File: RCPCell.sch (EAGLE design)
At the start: 28 parts, among them IC1 SIM900, U1 PESDXS4UD, U7 FAN8303

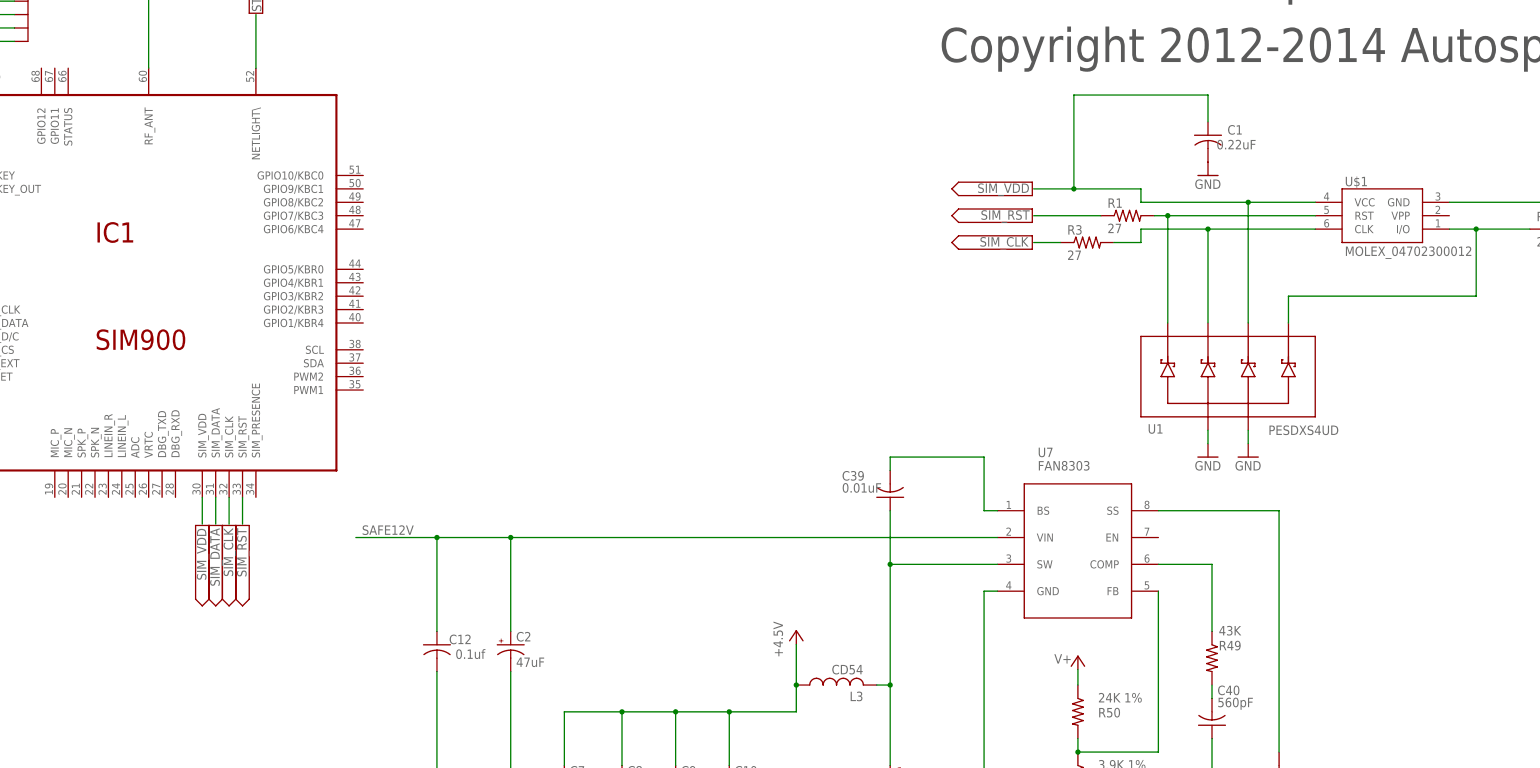
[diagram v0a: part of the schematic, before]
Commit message: flipped components on cell module to top side
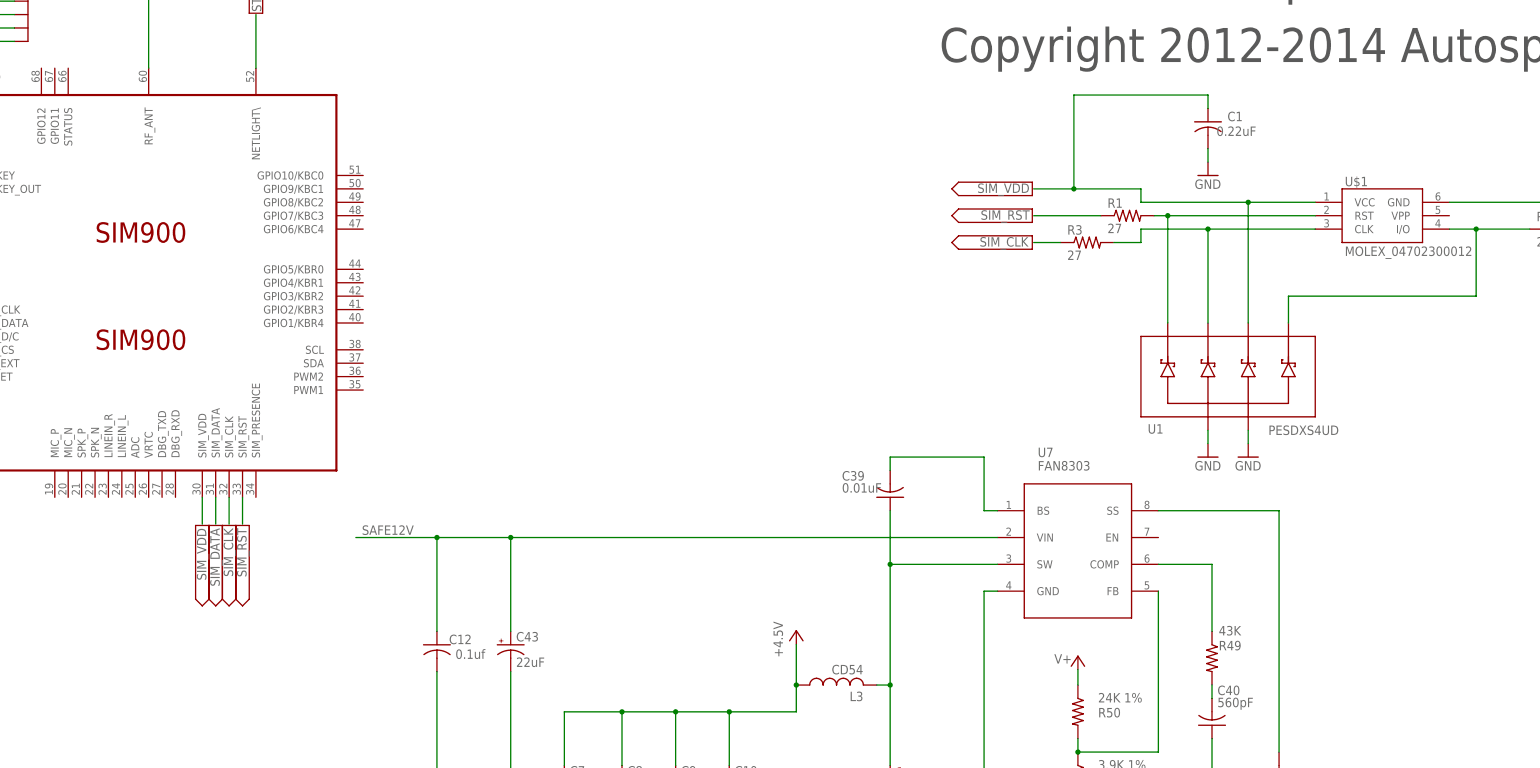
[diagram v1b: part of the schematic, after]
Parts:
- removed C2: 47uF, rcl:CPOL-USSMCD
- added C43: 22uF, rcl:CPOL-US153CLV-0605
- renumbered IC1 to SIM900
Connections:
- removed net N$2: C1.2, EX1.1, EX2.1, EX2.2, J$1.GND@0, J$1.GND@1, J$1.GND@2, J$1.GND@3, R8.1, SIM900GND@1.GND, SIM900GND@10.GND, SIM900GND@11.GND, SIM900GND@12.GND, SIM900GND@13.GND, SIM900GND@14.GND, SIM900GND@15.GND, SIM900GND@2.GND, SIM900GND@3.GND, SIM900GND@4.GND, SIM900GND@5.GND, SIM900GND@6.GND, SIM900GND@7.GND, SIM900GND@8.GND, SIM900GND@9.GND, U$1.GND, U1.2, U1.5
- net GND: now also C1.2, C43.-, EX1.1, EX2.1, EX2.2, J$1.GND@0, J$1.GND@1, J$1.GND@2, J$1.GND@3, R8.1, SIM900GND@1.GND, SIM900GND@10.GND, SIM900GND@11.GND, SIM900GND@12.GND, SIM900GND@13.GND, SIM900GND@14.GND, SIM900GND@15.GND, SIM900GND@2.GND, SIM900GND@3.GND, SIM900GND@4.GND, SIM900GND@5.GND, SIM900GND@6.GND, SIM900GND@7.GND, SIM900GND@8.GND, SIM900GND@9.GND, U$1.GND, U1.2, U1.5; no longer C2.-
- net SAFE12V: now also C43.+; no longer C2.+
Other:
- moved on the sheet: C1

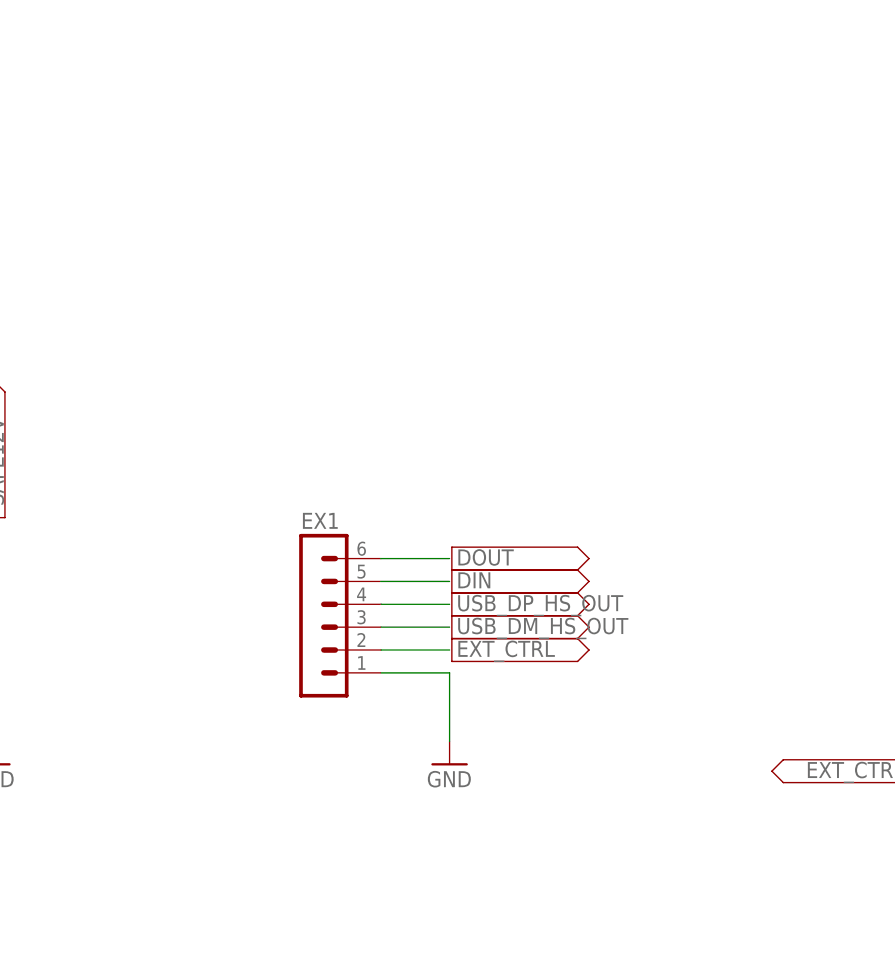
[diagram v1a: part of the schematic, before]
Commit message: fixed flipped routing on I/O header
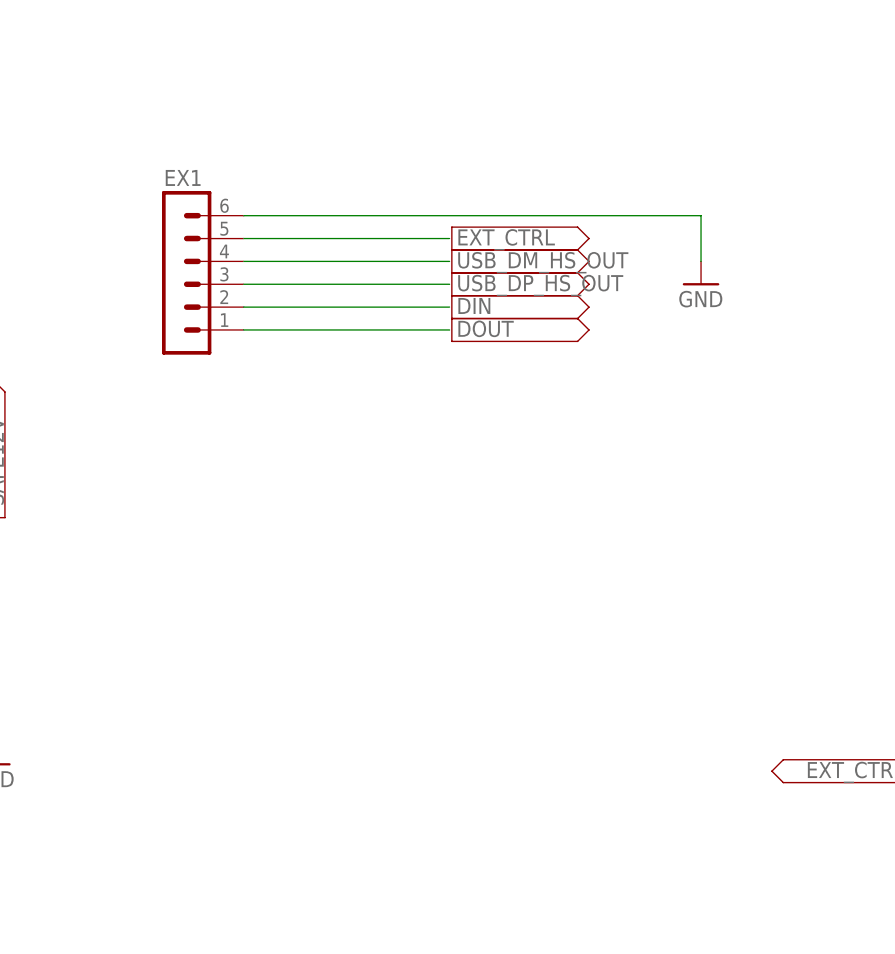
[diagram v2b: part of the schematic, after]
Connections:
- net DIN: now also EX1.2; no longer EX1.5
- net DOUT: now also EX1.1; no longer EX1.6
- net EXT_CTRL: now also EX1.5; no longer EX1.2
- net GND: now also EX1.6; no longer EX1.1
- net USB_DM_HS_OUT: now also EX1.4; no longer EX1.3
- net USB_DP_HS_OUT: now also EX1.3; no longer EX1.4
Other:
- moved on the sheet: EX1
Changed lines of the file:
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@@
 <setting verticaltext="up"/>
 </settings>
-<grid distance="0.005" unitdist="inch" unit="inch" style="lines" multiple="1" display="no" altdistance="0.01" altunitdist="inch" altunit="inch"/>
+<grid distance="0.1" unitdist="inch" unit="inch" style="lines" multiple="1" display="no" altdistance="0.01" altunitdist="inch" altunit="inch"/>
 <layers>
 <layer number="1" name="Top" color="4" fill="1" visible="no" active="no"/>
@@
 <instance part="U1" gate="G$1" x="109.22" y="111.76"/>
 <instance part="GND10" gate="1" x="111.76" y="96.52"/>
-<instance part="EX1" gate="1" x="-114.3" y="0"/>
+<instance part="EX1" gate="1" x="-129.54" y="38.1"/>
 <instance part="EX2" gate="1" x="-165.1" y="0"/>
-<instance part="AD33" gate="G$1" x="-98.806" y="5.08" smashed="yes">
-<attribute name="VALUE" x="-97.536" y="4.318" size="1.778" layer="96"/>
-</instance>
-<instance part="AD54" gate="G$1" x="-98.806" y="2.54" smashed="yes">
-<attribute name="VALUE" x="-97.536" y="1.778" size="1.778" layer="96"/>
-</instance>
-<instance part="AD137" gate="G$1" x="-98.806" y="0" smashed="yes">
-<attribute name="VALUE" x="-97.536" y="-0.762" size="1.778" layer="96"/>
-</instance>
-<instance part="AD151" gate="G$1" x="-98.806" y="-2.54" smashed="yes">
-<attribute name="VALUE" x="-97.536" y="-3.302" size="1.778" layer="96"/>
-</instance>
-<instance part="GND82" gate="1" x="-99.06" y="-17.78"/>
+<instance part="AD33" gate="G$1" x="-98.806" y="30.48" smashed="yes">
+<attribute name="VALUE" x="-97.536" y="29.718" size="1.778" layer="96"/>
+</instance>
+<instance part="AD54" gate="G$1" x="-98.806" y="33.02" smashed="yes">
+<attribute name="VALUE" x="-97.536" y="32.258" size="1.778" layer="96"/>
+</instance>
+<instance part="AD137" gate="G$1" x="-98.806" y="35.56" smashed="yes">
+<attribute name="VALUE" x="-97.536" y="34.798" size="1.778" layer="96"/>
+</instance>
+<instance part="AD151" gate="G$1" x="-98.806" y="38.1" smashed="yes">
+<attribute name="VALUE" x="-97.536" y="37.338" size="1.778" layer="96"/>
+</instance>
+<instance part="GND82" gate="1" x="-71.12" y="35.56"/>
 <instance part="GND83" gate="1" x="-149.86" y="-17.78"/>
 <instance part="AD156" gate="G$1" x="-149.733" y="9.6266" smashed="yes" rot="R90">
@@
 <attribute name="VALUE" x="78.359" y="59.182" size="1.778" layer="96" rot="R180"/>
 </instance>
-<instance part="AD1" gate="G$1" x="-98.806" y="-5.08" smashed="yes">
-<attribute name="VALUE" x="-97.536" y="-5.842" size="1.778" layer="96"/>
+<instance part="AD1" gate="G$1" x="-98.806" y="40.64" smashed="yes">
+<attribute name="VALUE" x="-97.536" y="39.878" size="1.778" layer="96"/>
 </instance>
 <instance part="R4" gate="G$1" x="-33.782" y="-18.542" rot="R180"/>
@@
 </segment>
 <segment>
-<pinref part="EX1" gate="1" pin="5"/>
-<wire x1="-106.68" y1="2.54" x2="-99.06" y2="2.54" width="0.1524" layer="91"/>
-<label x="-98.298" y="1.778" size="1.778" layer="95"/>
+<wire x1="-121.92" y1="33.02" x2="-99.06" y2="33.02" width="0.1524" layer="91"/>
+<label x="-98.298" y="32.258" size="1.778" layer="95"/>
+<pinref part="EX1" gate="1" pin="2"/>
 </segment>
 </net>
@@
 </segment>
 <segment>
-<pinref part="EX1" gate="1" pin="6"/>
-<wire x1="-106.68" y1="5.08" x2="-99.06" y2="5.08" width="0.1524" layer="91"/>
-<label x="-98.298" y="4.318" size="1.778" layer="95"/>
+<wire x1="-121.92" y1="30.48" x2="-99.06" y2="30.48" width="0.1524" layer="91"/>
+<label x="-98.298" y="29.718" size="1.778" layer="95"/>
+<pinref part="EX1" gate="1" pin="1"/>
 </segment>
 </net>
@@
 <net name="USB_DM_HS_OUT" class="0">
 <segment>
-<pinref part="EX1" gate="1" pin="3"/>
-<wire x1="-106.68" y1="-2.54" x2="-99.06" y2="-2.54" width="0.1524" layer="91"/>
-<label x="-98.298" y="-3.302" size="1.778" layer="95"/>
+<wire x1="-121.92" y1="38.1" x2="-99.06" y2="38.1" width="0.1524" layer="91"/>
+<label x="-98.298" y="37.338" size="1.778" layer="95"/>
+<pinref part="EX1" gate="1" pin="4"/>
 </segment>
 </net>
 <net name="USB_DP_HS_OUT" class="0">
 <segment>
-<pinref part="EX1" gate="1" pin="4"/>
-<wire x1="-106.68" y1="0" x2="-99.06" y2="0" width="0.1524" layer="91"/>
-<label x="-98.298" y="-0.762" size="1.778" layer="95"/>
+<wire x1="-121.92" y1="35.56" x2="-99.06" y2="35.56" width="0.1524" layer="91"/>
+<label x="-98.298" y="34.798" size="1.778" layer="95"/>
+<pinref part="EX1" gate="1" pin="3"/>
 </segment>
 </net>
@@
 <net name="EXT_CTRL" class="0">
 <segment>
-<pinref part="EX1" gate="1" pin="2"/>
-<wire x1="-106.68" y1="-5.08" x2="-99.06" y2="-5.08" width="0.1524" layer="91"/>
-<label x="-98.298" y="-5.842" size="1.778" layer="95"/>
+<wire x1="-121.92" y1="40.64" x2="-99.06" y2="40.64" width="0.1524" layer="91"/>
+<label x="-98.298" y="39.878" size="1.778" layer="95"/>
+<pinref part="EX1" gate="1" pin="5"/>
 </segment>
 <segment>
@@
 </segment>
 <segment>
-<pinref part="EX1" gate="1" pin="1"/>
-<wire x1="-106.68" y1="-7.62" x2="-99.06" y2="-7.62" width="0.1524" layer="91"/>
-<wire x1="-99.06" y1="-7.62" x2="-99.06" y2="-15.24" width="0.1524" layer="91"/>
+<wire x1="-121.92" y1="43.18" x2="-71.12" y2="43.18" width="0.1524" layer="91"/>
+<wire x1="-71.12" y1="43.18" x2="-71.12" y2="38.1" width="0.1524" layer="91"/>
 <pinref part="GND82" gate="1" pin="GND"/>
-</segment>
-<segment>
+<pinref part="EX1" gate="1" pin="6"/>
+</segment>
+<segment>
